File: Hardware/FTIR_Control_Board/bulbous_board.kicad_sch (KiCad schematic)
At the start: 29 parts, among them J1 RJ45_LED_Shielded, Q1 NMOS, U1 TSR_1-2450, U2 Peensy4.1_DEV-16771, U3 TMC2208

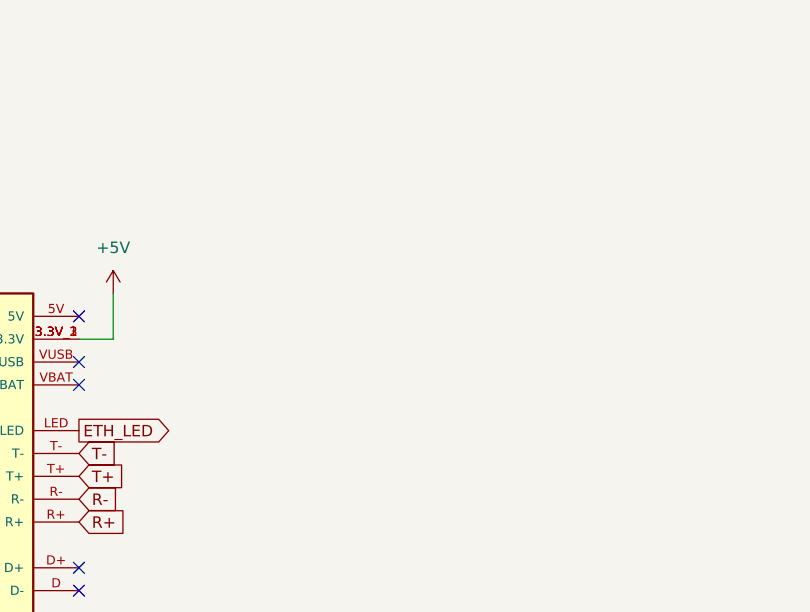
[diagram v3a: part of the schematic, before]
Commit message: Added TIA
Transimpedence Amp for Photodetector
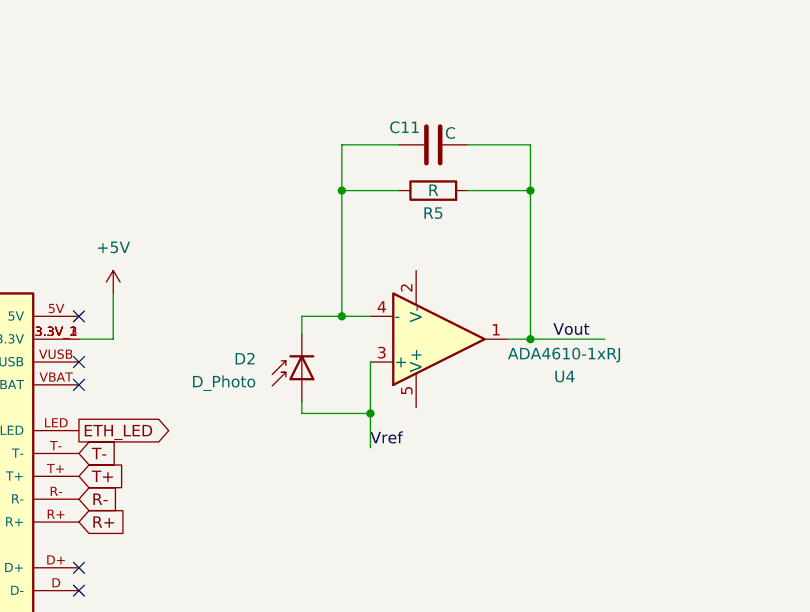
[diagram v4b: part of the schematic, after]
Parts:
- added C11: C, symbol Device:C
- added D2: D_Photo, symbol Device:D_Photo
- added R5: R, symbol Device:R
- added U4: ADA4610-1xRJ, Package_TO_SOT_SMD:SOT-23-5, symbol Amplifier_Operational:ADA4610-1xRJ
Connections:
- new net: C11.1, D2.1 (K), R5.1, U4.4 (-)
- new net Vout: C11.2, R5.2, U4.1
- new net Vref: D2.2 (A), U4.3 (+)
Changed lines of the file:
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@@
   (junction (at 271.145 53.975) (diameter 0) (color 0 0 0 0)
   )
+  (junction (at 188.595 37.465) (diameter 0) (color 0 0 0 0)
+  )
   (junction (at 224.155 146.05) (diameter 0) (color 0 0 0 0)
   )
@@
   (junction (at 252.095 120.015) (diameter 0) (color 0 0 0 0)
   )
+  (junction (at 209.55 37.465) (diameter 0) (color 0 0 0 0)
+  )
   (junction (at 55.245 33.02) (diameter 0) (color 0 0 0 0)
   )
@@
   (junction (at 243.205 108.585) (diameter 0) (color 0 0 0 0)
   )
+  (junction (at 188.595 51.435) (diameter 0) (color 0 0 0 0)
+  )
   (junction (at 238.125 120.015) (diameter 0) (color 0 0 0 0)
   )
@@
   (junction (at 197.485 146.05) (diameter 0) (color 0 0 0 0)
   )
+  (junction (at 209.55 53.975) (diameter 0) (color 0 0 0 0)
+  )
   (junction (at 244.475 137.795) (diameter 0) (color 0 0 0 0)
+  )
+  (junction (at 191.77 62.23) (diameter 0) (color 0 0 0 0)
   )
   (no_connect (at 159.385 135.255))
@@
     (stroke (width 0) (type default))
   )
+  (wire (pts (xy 207.01 53.975) (xy 209.55 53.975))
+    (stroke (width 0) (type default))
+  )
   (wire (pts (xy 255.905 42.545) (xy 255.905 50.165))
     (stroke (width 0) (type default))
   )
   (wire (pts (xy 159.385 53.975) (xy 163.195 53.975))
+    (stroke (width 0) (type default))
+  )
+  (wire (pts (xy 202.565 32.385) (xy 209.55 32.385))
     (stroke (width 0) (type default))
   )
@@
     (stroke (width 0) (type default))
   )
+  (wire (pts (xy 184.15 60.96) (xy 184.15 62.23))
+    (stroke (width 0) (type default))
+  )
   (wire (pts (xy 252.095 118.745) (xy 252.095 120.015))
     (stroke (width 0) (type default))
@@
     (stroke (width 0) (type default))
   )
+  (wire (pts (xy 209.55 53.975) (xy 217.805 53.975))
+    (stroke (width 0) (type default))
+  )
   (wire (pts (xy 216.535 101.6) (xy 216.535 113.665))
     (stroke (width 0) (type default))
@@
     (stroke (width 0) (type default))
   )
+  (wire (pts (xy 202.565 37.465) (xy 209.55 37.465))
+    (stroke (width 0) (type default))
+  )
   (wire (pts (xy 79.375 33.02) (xy 83.185 33.02))
     (stroke (width 0) (type default))
@@
     (stroke (width 0) (type default))
   )
+  (wire (pts (xy 194.945 37.465) (xy 188.595 37.465))
+    (stroke (width 0) (type default))
+  )
   (wire (pts (xy 211.455 109.22) (xy 208.28 109.22))
     (stroke (width 0) (type default))
@@
   )
   (wire (pts (xy 252.095 111.125) (xy 252.095 108.585))
+    (stroke (width 0) (type default))
+  )
+  (wire (pts (xy 209.55 32.385) (xy 209.55 37.465))
     (stroke (width 0) (type default))
   )
@@
     (stroke (width 0) (type default))
   )
+  (wire (pts (xy 191.77 62.23) (xy 191.77 66.04))
+    (stroke (width 0) (type default))
+  )
+  (wire (pts (xy 188.595 32.385) (xy 188.595 37.465))
+    (stroke (width 0) (type default))
+  )
   (wire (pts (xy 69.215 40.64) (xy 69.215 43.18))
+    (stroke (width 0) (type default))
+  )
+  (wire (pts (xy 184.15 51.435) (xy 188.595 51.435))
     (stroke (width 0) (type default))
   )
@@
     (stroke (width 0) (type dash))
   )
+  (wire (pts (xy 194.945 32.385) (xy 188.595 32.385))
+    (stroke (width 0) (type default))
+  )
   (wire (pts (xy 193.675 127.635) (xy 200.025 127.635))
     (stroke (width 0) (type default))
@@
     (stroke (width 0) (type default))
   )
+  (wire (pts (xy 188.595 37.465) (xy 188.595 51.435))
+    (stroke (width 0) (type default))
+  )
   (wire (pts (xy 232.41 132.715) (xy 255.905 132.715))
     (stroke (width 0) (type default))
@@
     (stroke (width 0) (type default))
   )
+  (wire (pts (xy 209.55 37.465) (xy 209.55 53.975))
+    (stroke (width 0) (type default))
+  )
   (wire (pts (xy 255.905 126.365) (xy 255.905 125.095))
     (stroke (width 0) (type default))
   )
+  (wire (pts (xy 188.595 51.435) (xy 191.77 51.435))
+    (stroke (width 0) (type default))
+  )
   (wire (pts (xy 208.28 97.155) (xy 210.185 97.155))
     (stroke (width 0) (type default))
@@
     (stroke (width 0) (type default))
   )
+  (wire (pts (xy 184.15 53.34) (xy 184.15 51.435))
+    (stroke (width 0) (type default))
+  )
+  (wire (pts (xy 184.15 62.23) (xy 191.77 62.23))
+    (stroke (width 0) (type default))
+  )
   (wire (pts (xy 268.605 19.685) (xy 268.605 22.225))
     (stroke (width 0) (type default))
@@
   )
   (wire (pts (xy 219.075 101.6) (xy 216.535 101.6))
+    (stroke (width 0) (type default))
+  )
+  (wire (pts (xy 191.77 62.23) (xy 191.77 56.515))
     (stroke (width 0) (type default))
   )
@@
   )
   (text "Photodetector Break-away" (at 24.765 128.27 0)
+    (effects (font (size 1.27 1.27)) (justify left bottom))
+  )
+  (label "Vref" (at 191.77 66.04 0) (fields_autoplaced)
+    (effects (font (size 1.27 1.27)) (justify left bottom))
+  )
+  (label "Vout" (at 212.09 53.975 0) (fields_autoplaced)
     (effects (font (size 1.27 1.27)) (justify left bottom))
   )
@@
     )
   )
+  (symbol (lib_id "Device:C") (at 198.755 32.385 90) (unit 1)
+    (in_bom yes) (on_board yes) (dnp no)
+    (property "Reference" "C11" (at 195.58 30.48 90)
+      (effects (font (size 1.27 1.27)))
+    )
+    (property "Value" "C" (at 200.66 31.115 90)
+      (effects (font (size 1.27 1.27)))
+    )
+    (property "Footprint" "" (at 202.565 31.4198 0)
+      (effects (font (size 1.27 1.27)) hide)
+    )
+    (property "Datasheet" "~" (at 198.755 32.385 0)
+      (effects (font (size 1.27 1.27)) hide)
+    )
+    (pin "1")
+    (pin "2")
+    (instances
+      (project "bulbous_board"
+        (path "/049c3f09-c046-40c3-9872-e62b40667976"
+          (reference "C11") (unit 1)
+        )
+      )
+    )
+  )
   (symbol (lib_id "Device:C") (at 252.095 50.165 270) (unit 1)
     (in_bom yes) (on_board yes) (dnp no)
@@
     )
   )
+  (symbol (lib_id "Amplifier_Operational:ADA4610-1xRJ") (at 199.39 53.975 0) (mirror x) (unit 1)
+    (in_bom yes) (on_board yes) (dnp no)
+    (property "Reference" "U4" (at 213.36 58.1659 0)
+      (effects (font (size 1.27 1.27)))
+    )
+    (property "Value" "ADA4610-1xRJ" (at 213.36 55.6259 0)
+      (effects (font (size 1.27 1.27)))
+    )
+    (property "Footprint" "Package_TO_SOT_SMD:SOT-23-5" (at 196.85 48.895 0)
+      (effects (font (size 1.27 1.27)) (justify left) hide)
+    )
+    (property "Datasheet" "https://www.analog.com/media/en/technical-documentation/data-sheets/ADA4610-1_4610-2_4610-4.pdf" (at 199.39 59.055 0)
+      (effects (font (size 1.27 1.27)) hide)
+    )
+    (pin "2")
+    (pin "5")
+    (pin "1")
+    (pin "3")
+    (pin "4")
+    (instances
+      (project "bulbous_board"
+        (path "/049c3f09-c046-40c3-9872-e62b40667976"
+          (reference "U4") (unit 1)
+        )
+      )
+    )
+  )
   (symbol (lib_id "Device:C") (at 204.47 109.22 90) (unit 1)
     (in_bom yes) (on_board yes) (dnp no)
@@
         (path "/049c3f09-c046-40c3-9872-e62b40667976"
           (reference "RV1") (unit 1)
+        )
+      )
+    )
+  )
+  (symbol (lib_id "Device:D_Photo") (at 184.15 58.42 90) (mirror x) (unit 1)
+    (in_bom yes) (on_board yes) (dnp no)
+    (property "Reference" "D2" (at 179.07 56.1975 90)
+      (effects (font (size 1.27 1.27)) (justify left))
+    )
+    (property "Value" "D_Photo" (at 179.07 58.7375 90)
+      (effects (font (size 1.27 1.27)) (justify left))
+    )
+    (property "Footprint" "" (at 184.15 57.15 0)
+      (effects (font (size 1.27 1.27)) hide)
+    )
+    (property "Datasheet" "~" (at 184.15 57.15 0)
+      (effects (font (size 1.27 1.27)) hide)
+    )
+    (pin "1")
+    (pin "2")
+    (instances
+      (project "bulbous_board"
+        (path "/049c3f09-c046-40c3-9872-e62b40667976"
+          (reference "D2") (unit 1)
         )
       )
@@
         )
       )
+    )
+  )
+  (symbol (lib_id "Device:R") (at 198.755 37.465 90) (unit 1)
+    (in_bom yes) (on_board yes) (dnp no)
+    (property "Reference" "R5" (at 198.755 40.005 90)
+      (effects (font (size 1.27 1.27)))
+    )
+    (property "Value" "R" (at 198.755 37.465 90)
+      (effects (font (size 1.27 1.27)))
+    )
+    (property "Footprint" "" (at 198.755 39.243 90)
+      (effects (font (size 1.27 1.27)) hide)
+    )
+    (property "Datasheet" "~" (at 198.755 37.465 0)
+      (effects (font (size 1.27 1.27)) hide)
+    )
+    (pin "1")
+    (pin "2")
+    (instances
+      (project "bulbous_board"
+        (path "/049c3f09-c046-40c3-9872-e62b40667976"
+          (reference "R5") (unit 1)
+        )
+      )

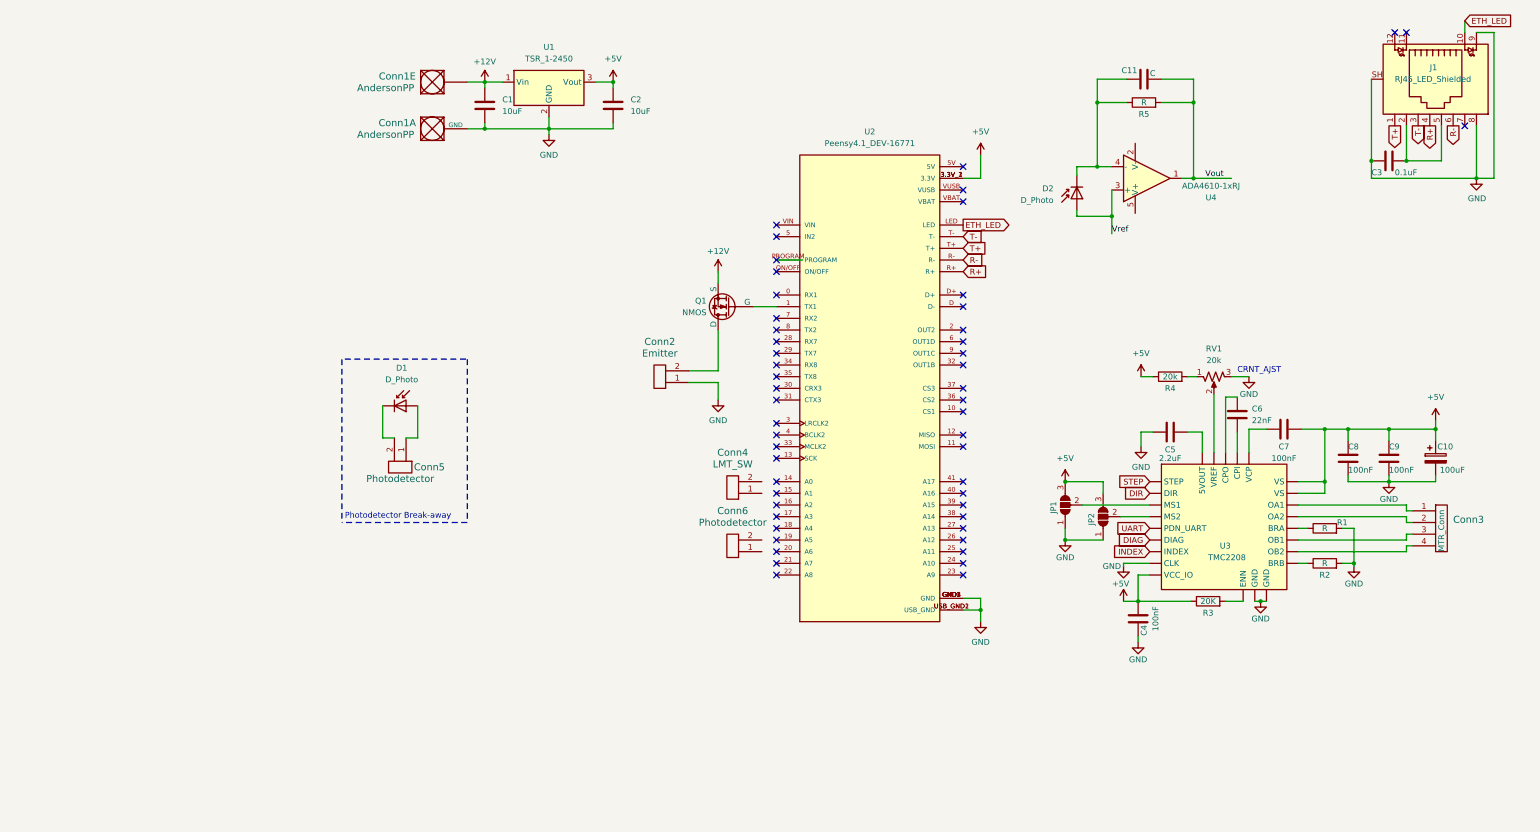
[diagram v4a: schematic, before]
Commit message: Improved MOSFET
Figured out how mosfet switches work
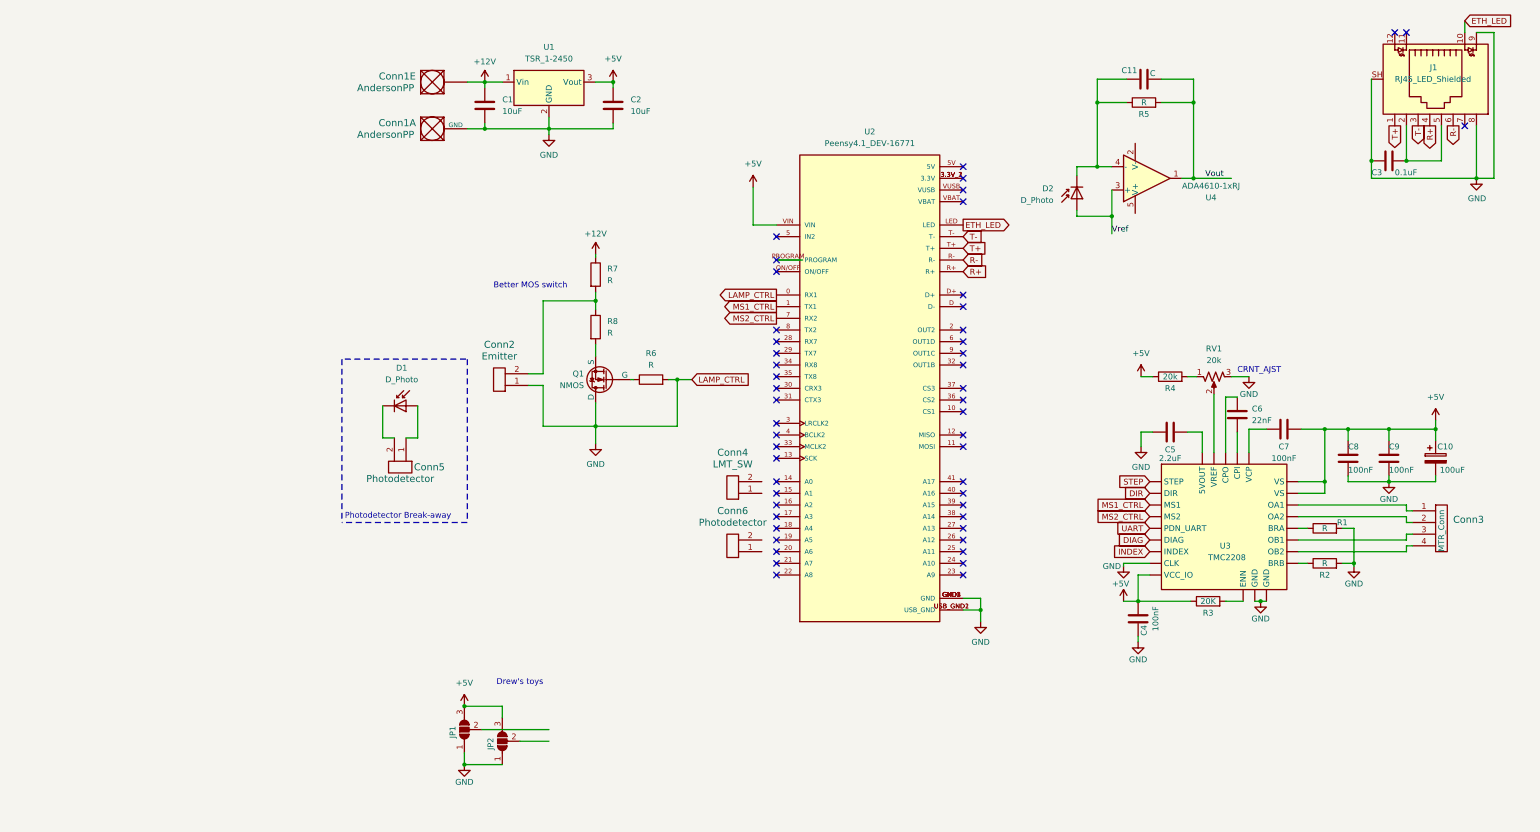
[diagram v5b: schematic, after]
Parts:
- added R6, R7, R8: R, symbol Device:R
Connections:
- net +12V: now also R7.1; no longer Q1.3 (S)
- net +5V: now also U2.VIN; no longer U2.3.3V_1 (3.3V), U2.3.3V_2 (3.3V), U2.3.3V_3 (3.3V)
- net GND: now also Q1.1 (D), U2.0 (RX1), R6.2
- net at JP2.2 (C): no longer U3. (VS)
- net at JP1.2 (C): no longer U3. (VS)
- net at Conn2.2: now also R7.2, R8.1; no longer Q1.1 (D)
- net at Q1.2 (G): now also R6.1; no longer U2.1 (TX1)
- net MS2_CTRL: now reaches U2.7 (RX2)
- net MS2_CTRL: now also U3. (VS)
- new net: Q1.3 (S), R8.2
- new net: U2.3.3V_1 (3.3V), U2.3.3V_2 (3.3V), U2.3.3V_3 (3.3V)
- new net MS1_CTRL: U2.1 (TX1), U3. (VS)
- no-connect marks 52 -> 50
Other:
- note added: "Better MOS switch"
- note added: "Drew's toys"
- moved on the sheet: Conn2, JP1, JP2, Q1

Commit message: Stuff idk
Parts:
- removed Conn6: Photodetector, symbol MRDT_Connectors:Molex_SL_02
- added Conn7, Conn8: RP-SMA, symbol MRDT_Connectors:RP-SMA
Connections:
- net +5V: now also U4.2 (V-)
- net GND: now also U4.5 (V+), Conn7.2 (Sleve), Conn8.2 (Sleve)
- net at U2.22 (A8): now also Conn8.1 (Tip)
- net Vout: no longer names the net of C11.2, R5.2, U4.1
- net Vout: now also Conn7.1 (Tip)
- no-connect marks 50 -> 47
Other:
- moved on the sheet: C11, D2, R5, U4
